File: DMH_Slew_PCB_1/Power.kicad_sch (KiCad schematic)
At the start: 14 parts, among them J0 Conn_01x01, J100 IDC_02x05, J101 IDC_02x08

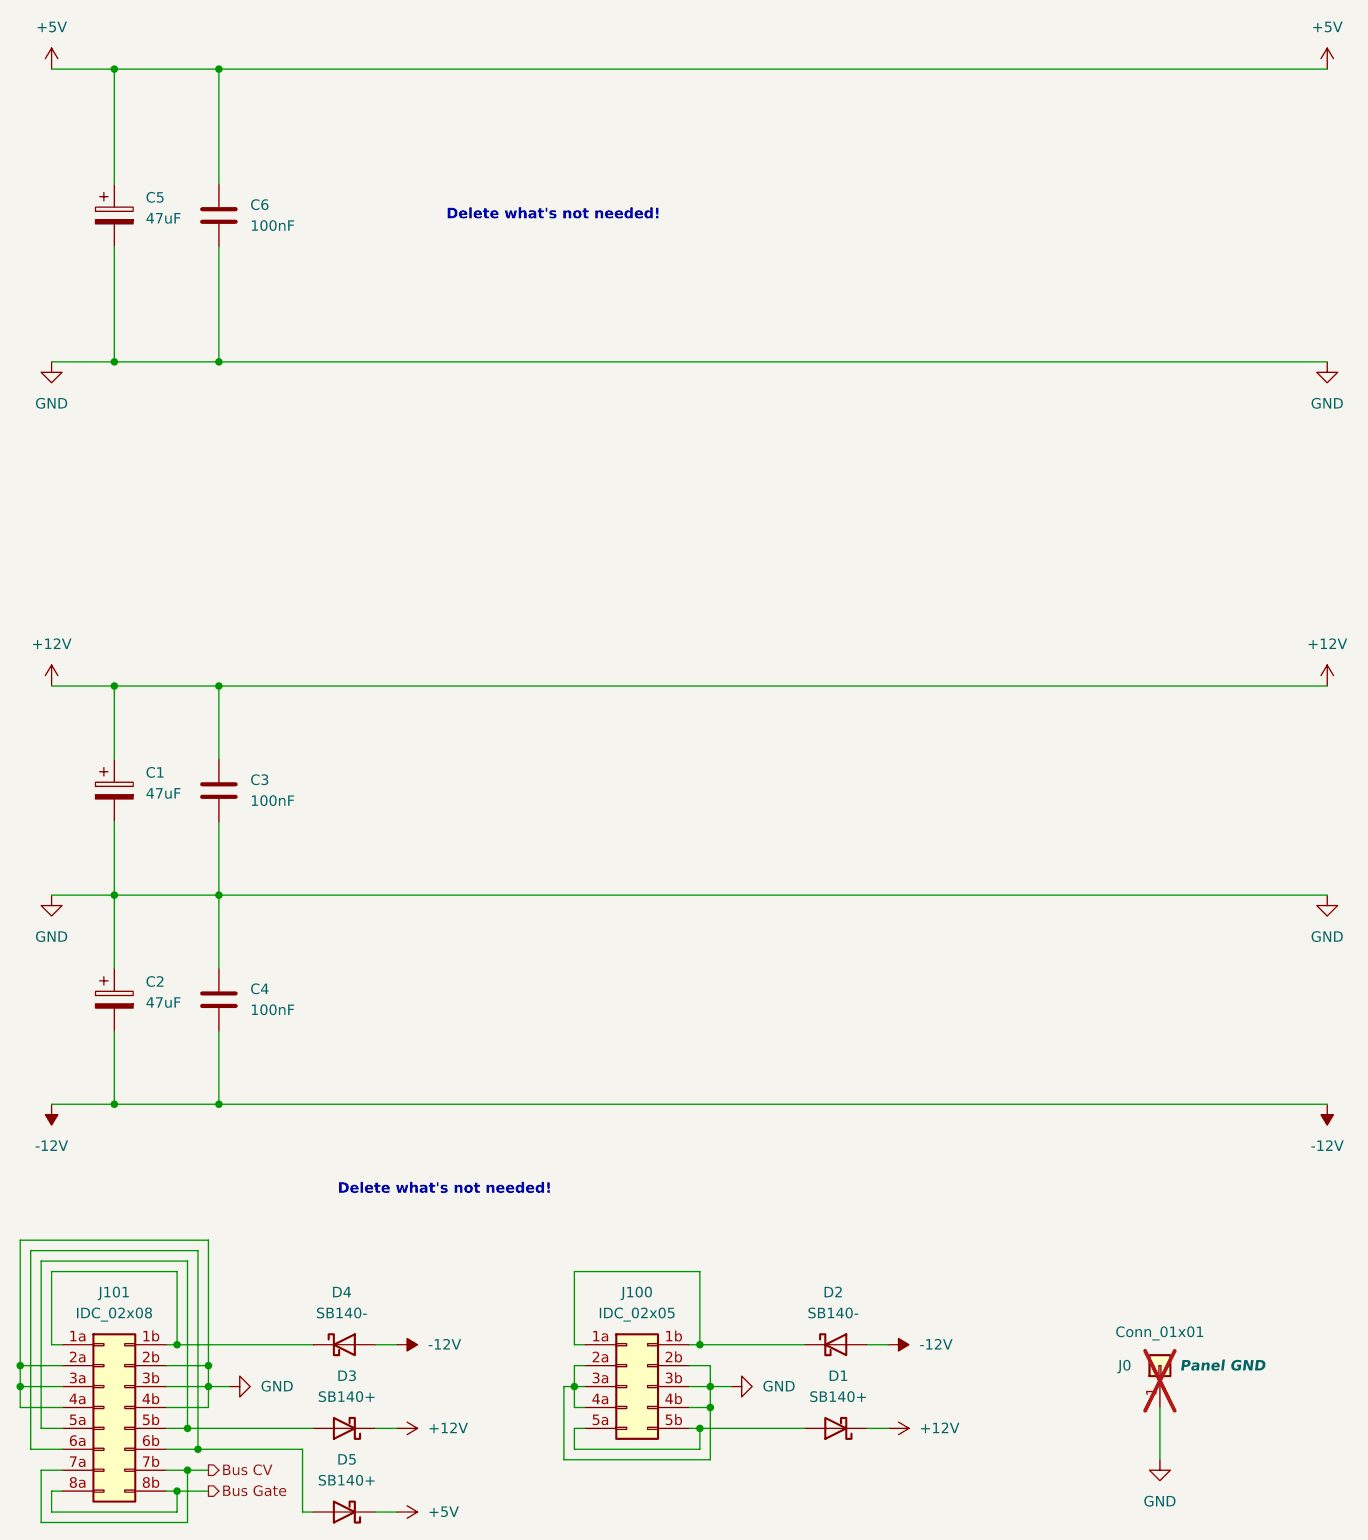
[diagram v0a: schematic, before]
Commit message: Designed IO page
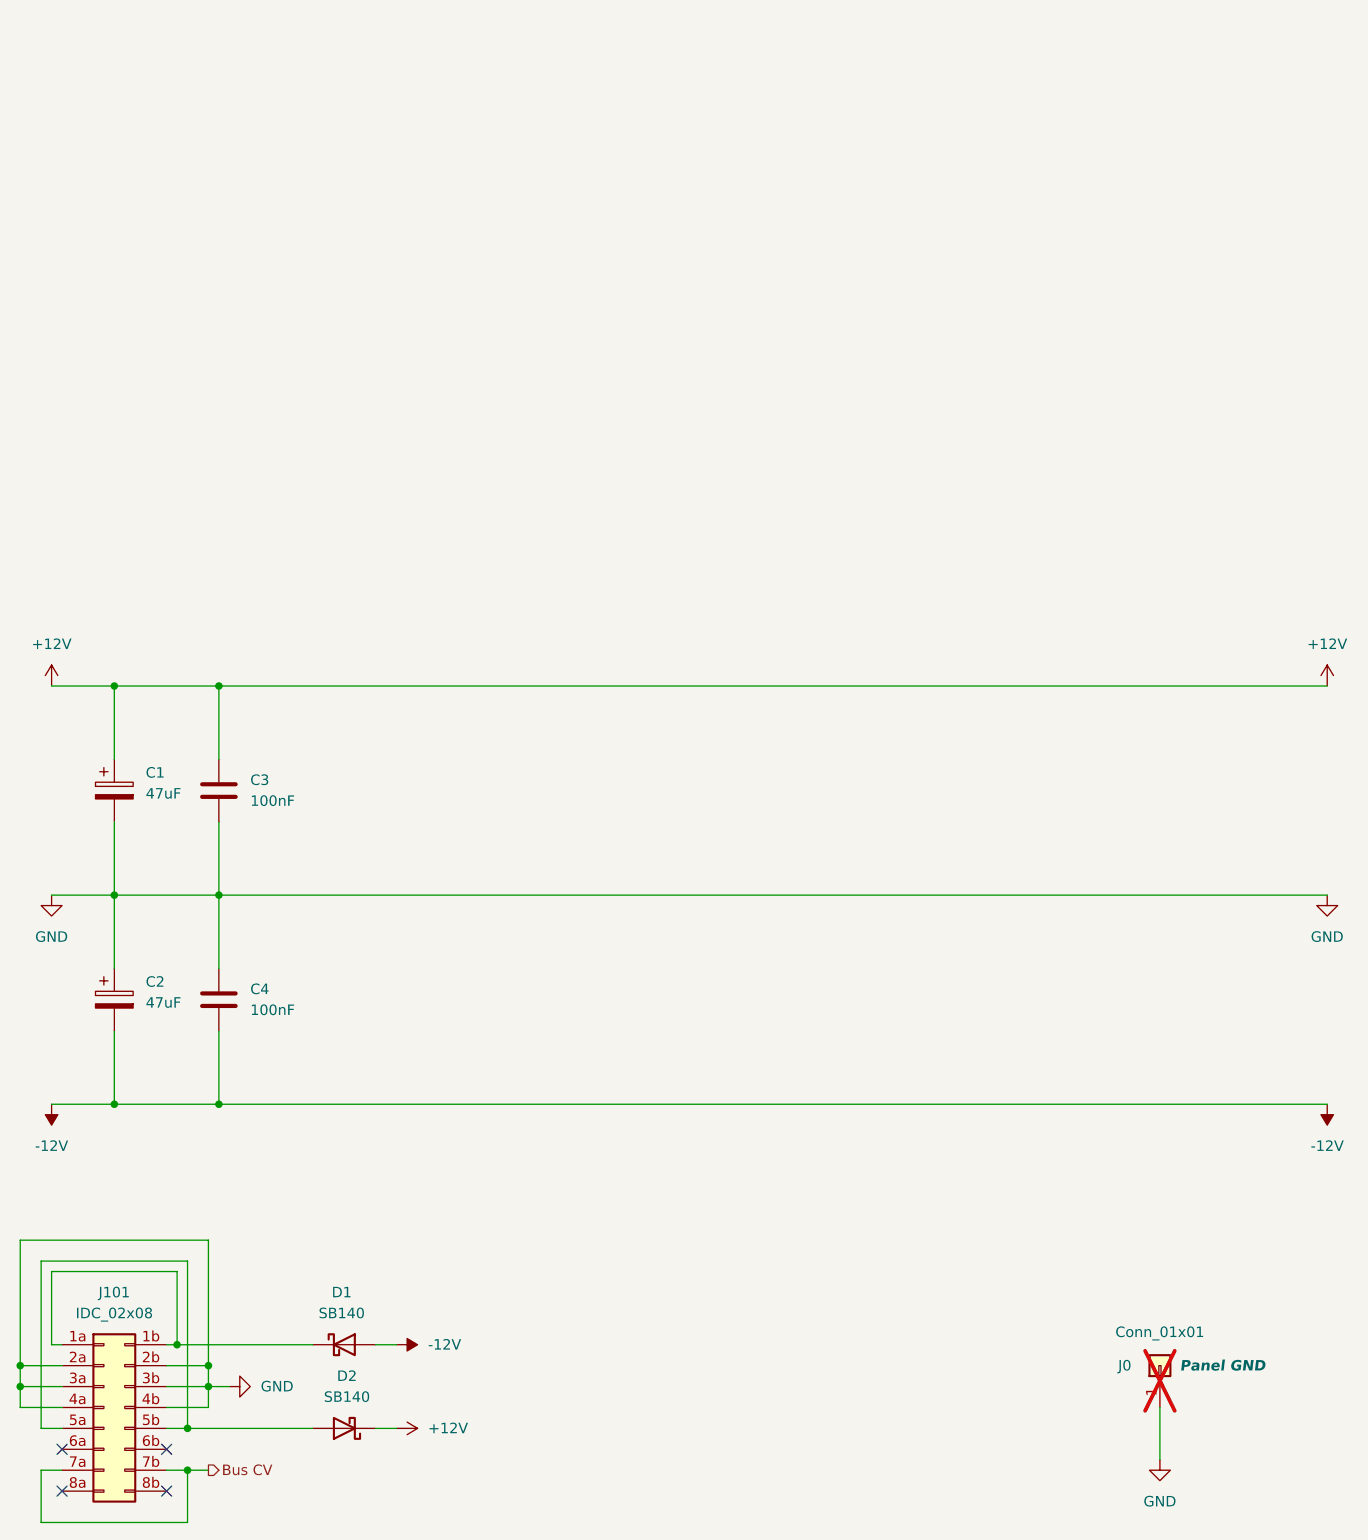
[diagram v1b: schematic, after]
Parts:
- removed C5: 47uF, Capacitor_THT:CP_Radial_D4.0mm_P1.50mm, symbol Device:C_Polarized
- removed C6: 100nF, Capacitor_THT:C_Disc_D4.3mm_W1.9mm_P5.00mm, symbol Device:C
- removed D1, D5: SB140+, Diode_THT:D_DO-41_SOD81_P10.16mm_Horizontal, symbol SynthStuff:Power_Bus_Schotty_+
- removed D2: SB140-, Diode_THT:D_DO-41_SOD81_P10.16mm_Horizontal, symbol SynthStuff:Power_Bus_Schotty_-
- removed J100: IDC_02x05, SynthStuff:IDC-Header_2x05_P2.54mm_Vertical_Eurorack, symbol SynthStuff:Eurorack_Power_Connector_10Pin
- D1: renamed from D4; value SB140- -> SB140
- D2: renamed from D3; value SB140+ -> SB140
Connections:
- net at J101.6a (Pin_6a): no longer J101.6b (Pin_6b)
- net Bus Gate: no longer names the net of J101.8a (Pin_8a)
- net Bus Gate: no longer J101.8b (Pin_8b)
- no-connect marks 0 -> 4
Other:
- note removed: "Delete what's not needed!"

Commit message: Finished power distribution
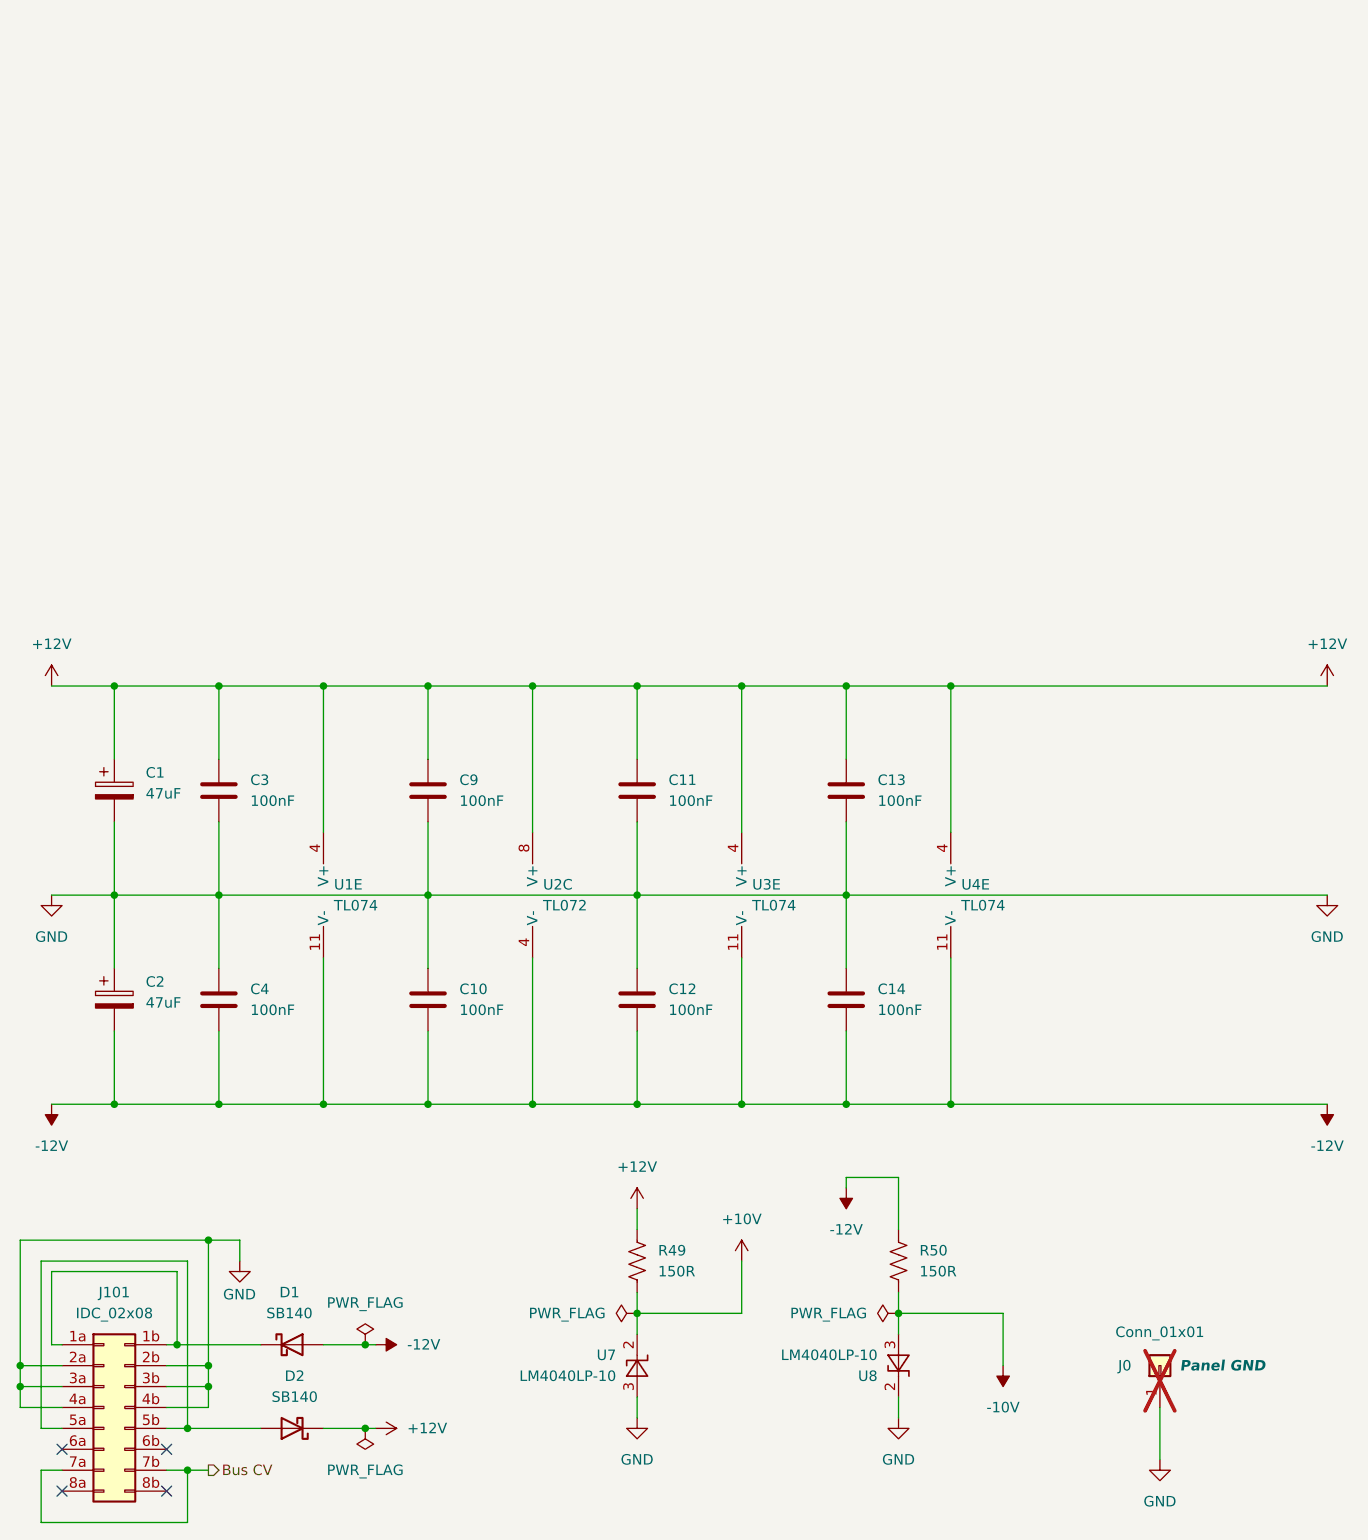
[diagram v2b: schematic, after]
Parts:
- removed D1: SB140, Diode_THT:D_DO-41_SOD81_P10.16mm_Horizontal, symbol SynthStuff:Power_Bus_Schotty_-
- removed D2: SB140, Diode_THT:D_DO-41_SOD81_P10.16mm_Horizontal, symbol SynthStuff:Power_Bus_Schotty_+
- added C10, C11, C12, C13, C14, C9: 100nF, Capacitor_THT:C_Disc_D4.3mm_W1.9mm_P5.00mm, symbol Device:C
- added D1, D2: SB140, Diode_THT:D_DO-41_SOD81_P10.16mm_Horizontal, symbol Diode:SB140
- added R49, R50: 150R, Resistor_THT:R_Axial_DIN0207_L6.3mm_D2.5mm_P7.62mm_Horizontal, symbol Device:R_US
- added U1, U3, U4: TL074, symbol Amplifier_Operational:TL074
- added U2: TL072, symbol Amplifier_Operational:TL072
- added U7, U8: LM4040LP-10, Package_TO_SOT_THT:TO-92_Inline, symbol Reference_Voltage:LM4040LP-10
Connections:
- net +12V: now also C11.1, C13.1, C9.1, D2.1 (K), R49.2, U1.4 (V+), U2.8 (V+), U3.4 (V+), U4.4 (V+)
- net -12V: now also C10.2, C12.2, C14.2, D1.2 (A), R50.2, U1.11 (V-), U2.4 (V-), U3.11 (V-), U4.11 (V-)
- net GND: now also C10.1, C11.2, C12.1, C13.2, C14.1, C9.2, U7.3 (A), U8.2 (K)
- net at J101.1a (Pin_1a), J101.1b (Pin_1b): now also D1.1 (K)
- net at J101.5a (Pin_5a), J101.5b (Pin_5b): now also D2.2 (A)
- new net +10V: R49.1, U7.2 (K)
- new net -10V: R50.1, U8.3 (A)

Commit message: Exported preliminary BoM
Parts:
- U1, U3, U4: footprint (none) -> Package_DIP:DIP-14_W7.62mm_Socket
- U2: footprint (none) -> Package_DIP:DIP-8_W7.62mm_Socket
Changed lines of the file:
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@@
 			)
 		)
-		(property "Footprint" ""
+		(property "Footprint" "Package_DIP:DIP-14_W7.62mm_Socket"
 			(at 128.27 118.11 0)
 			(effects
@@
 			)
 		)
-		(property "Footprint" ""
+		(property "Footprint" "Package_DIP:DIP-14_W7.62mm_Socket"
 			(at 102.87 118.11 0)
 			(effects
@@
 			)
 		)
-		(property "Footprint" ""
+		(property "Footprint" "Package_DIP:DIP-14_W7.62mm_Socket"
 			(at 52.07 118.11 0)
 			(effects
@@
 			)
 		)
-		(property "Footprint" ""
+		(property "Footprint" "Package_DIP:DIP-8_W7.62mm_Socket"
 			(at 78.74 120.65 0)
 			(effects
